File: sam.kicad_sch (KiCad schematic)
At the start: 46 parts, among them IC1 4164, IC15 MC6883, IC16 74LS244N, IC2 4164, IC3 4164, IC31 74LS02N, IC33 74LS138N, IC36 74LS132, IC37 GAL, IC4 4164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

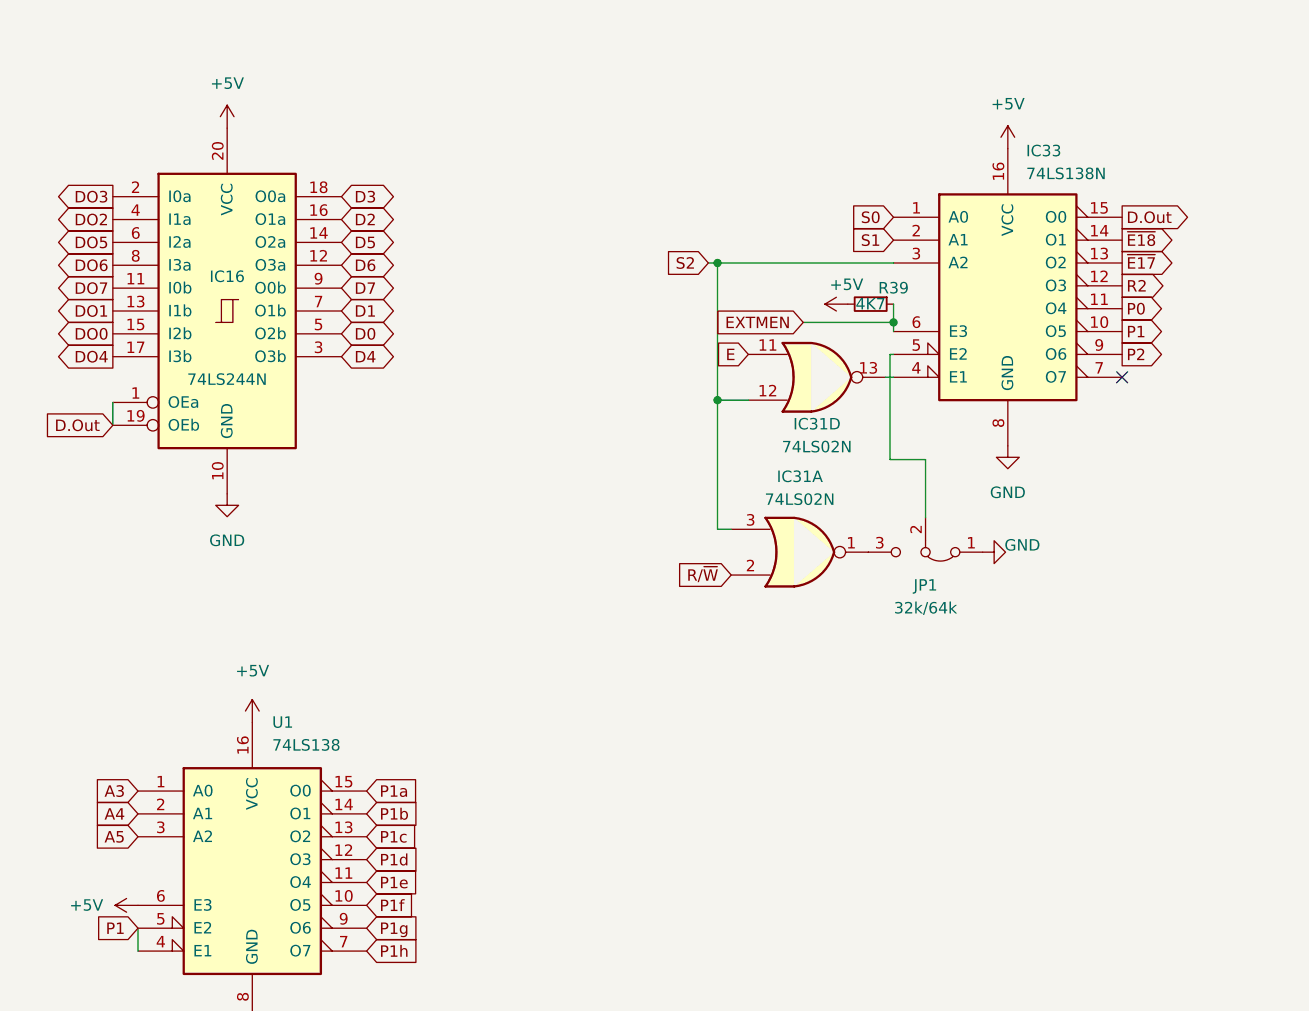
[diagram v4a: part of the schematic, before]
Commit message: fix rom and pia select traces
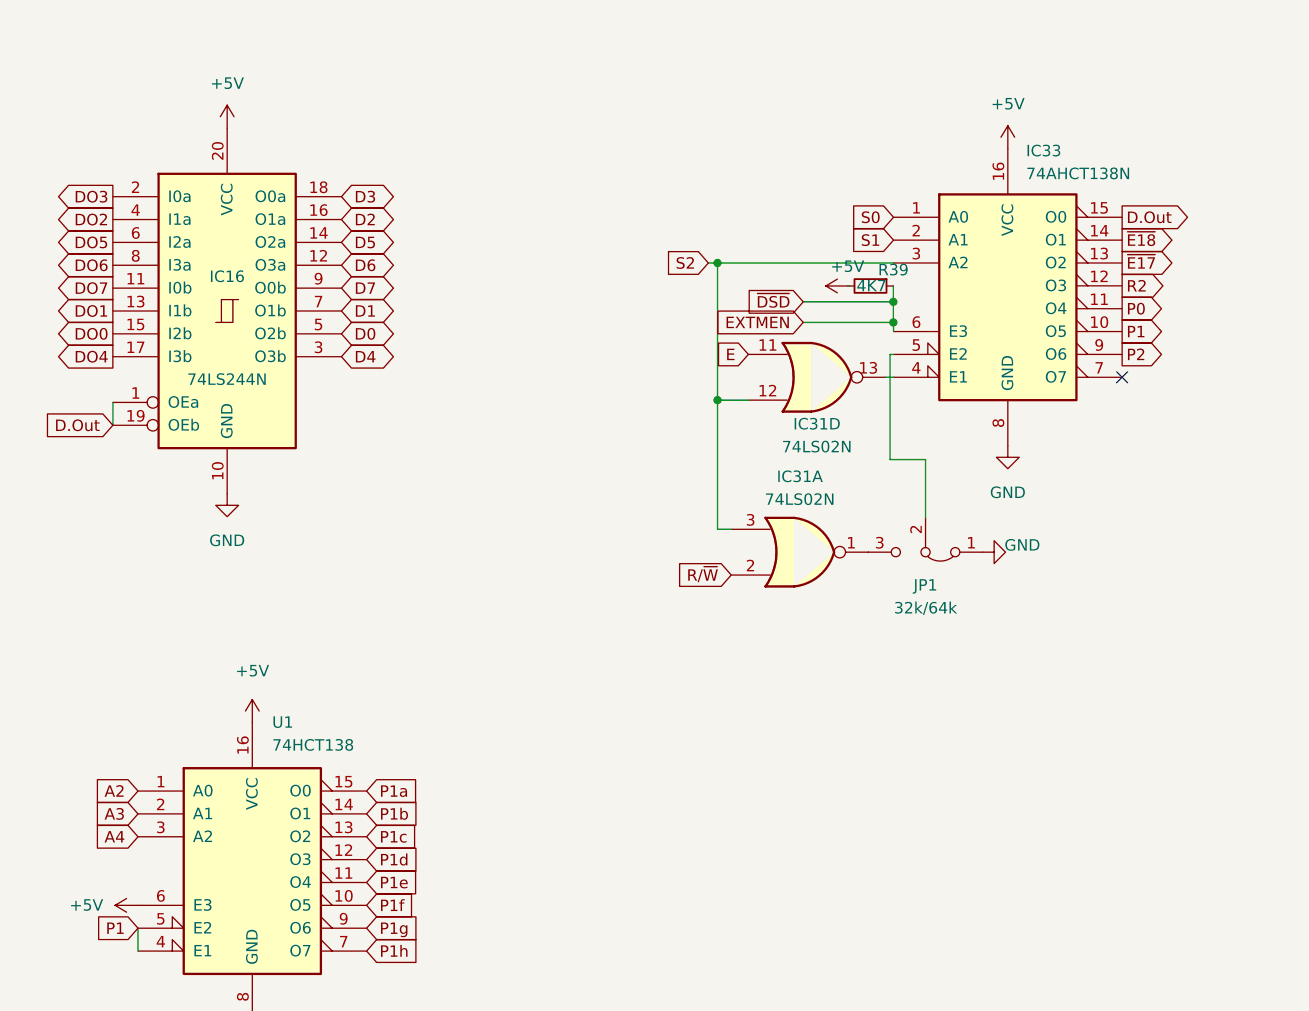
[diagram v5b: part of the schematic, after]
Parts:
- IC33: value 74LS138N -> 74AHCT138N
- JP5: footprint Jumper:SolderJumper-3_P1.3mm_Bridged12_Pad1.0x1.5mm -> Jumper:SolderJumper-3_P1.3mm_Open_Pad1.0x1.5mm
- U1: value 74LS138 -> 74HCT138
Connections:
- net ~{DSD} is gone; now on net EXTMEN: IC37.21 (IO2)
- net A2: now also U1.1 (A0)
- net A3: now also U1.2 (A1); no longer U1.1 (A0)
- net A4: now also U1.3 (A2); no longer U1.2 (A1)
- net A5: no longer U1.3 (A2)
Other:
- moved on the sheet: R39
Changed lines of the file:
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@@
     (comment 2 "Reposition dram and buffer")
   )
-  (junction (at 109.347 170.18) (diameter 0) (color 0 0 0 0)
+  (junction (at 109.3275 167.894) (diameter 0) (color 0 0 0 0)
   )
   (junction (at 66.929 24.638) (diameter 0) (color 0 0 0 0)
@@
   (junction (at 14.478 24.638) (diameter 0) (color 0 0 0 0)
   )
+  (junction (at 109.3275 170.18) (diameter 0) (color 0 0 0 0)
+  )
   (no_connect (at 134.747 176.276))
   (no_connect (at 259.842 177.292))
@@
     (stroke (width 0) (type default))
   )
+  (wire (pts (xy 99.314 167.894) (xy 109.3275 167.894))
+    (stroke (width 0) (type default))
+  )
   (wire (pts (xy 265.938 54.991) (xy 262.636 54.991))
     (stroke (width 0) (type default))
@@
     (stroke (width 0) (type default))
   )
+  (wire (pts (xy 109.3275 170.18) (xy 109.347 170.18))
+    (stroke (width 0) (type default))
+  )
   (wire (pts (xy 112.903 185.42) (xy 112.903 191.897))
     (stroke (width 0) (type default))
@@
     (stroke (width 0) (type default))
   )
+  (wire (pts (xy 104.3745 166.1319) (xy 104.2475 166.1319))
+    (stroke (width 0) (type default))
+  )
   (wire (pts (xy 93.218 178.816) (xy 89.789 178.816))
     (stroke (width 0) (type default))
@@
     (stroke (width 0) (type default))
   )
-  (wire (pts (xy 109.347 168.148) (xy 109.347 170.18))
+  (wire (pts (xy 109.3275 166.1319) (xy 109.3275 167.894))
     (stroke (width 0) (type default))
   )
@@
     (stroke (width 0) (type default))
   )
-  (wire (pts (xy 99.314 170.18) (xy 109.347 170.18))
+  (wire (pts (xy 109.3275 167.894) (xy 109.3275 170.18))
+    (stroke (width 0) (type default))
+  )
+  (wire (pts (xy 99.314 170.18) (xy 109.3275 170.18))
     (stroke (width 0) (type default))
   )
@@
     (stroke (width 0) (type default))
   )
-  (global_label "A5" (shape input) (at 25.4 227.33 180) (fields_autoplaced)
+  (global_label "A4" (shape input) (at 25.4 227.33 180) (fields_autoplaced)
     (effects (font (size 1.27 1.27)) (justify right))
     (property "Intersheetrefs" "${INTERSHEET_REFS}" (at 20.7709 227.33 0)
@@
     )
   )
+  (global_label "~{DSD}" (shape input) (at 99.314 167.894 180) (fields_autoplaced)
+    (effects (font (size 1.27 1.27)) (justify right))
+    (property "Intersheetrefs" "${INTERSHEET_REFS}" (at 93.2335 167.894 0)
+      (effects (font (size 1.27 1.27)) (justify right) hide)
+    )
+  )
   (global_label "RAM VCC" (shape passive) (at 168.148 146.431 0) (fields_autoplaced)
     (effects (font (size 1.27 1.27)) (justify left))
@@
     )
   )
-  (global_label "A3" (shape input) (at 25.4 222.25 180) (fields_autoplaced)
+  (global_label "A2" (shape input) (at 25.4 222.25 180) (fields_autoplaced)
     (effects (font (size 1.27 1.27)) (justify right))
     (property "Intersheetrefs" "${INTERSHEET_REFS}" (at 20.7709 222.25 0)
@@
     )
   )
-  (global_label "A4" (shape input) (at 25.4 224.79 180) (fields_autoplaced)
+  (global_label "A3" (shape input) (at 25.4 224.79 180) (fields_autoplaced)
     (effects (font (size 1.27 1.27)) (justify right))
     (property "Intersheetrefs" "${INTERSHEET_REFS}" (at 20.7709 224.79 0)
@@
       (effects (font (size 1.27 1.27)) (justify left))
     )
-    (property "Value" "74LS138" (at 40.2941 217.17 0)
+    (property "Value" "74HCT138" (at 40.2941 217.17 0)
       (effects (font (size 1.27 1.27)) (justify left))
     )
@@
       (effects (font (size 1.27 1.27)))
     )
-    (property "Footprint" "Jumper:SolderJumper-3_P1.3mm_Bridged12_Pad1.0x1.5mm" (at 207.518 39.116 0)
+    (property "Footprint" "Jumper:SolderJumper-3_P1.3mm_Open_Pad1.0x1.5mm" (at 207.518 39.116 0)
       (effects (font (size 1.27 1.27)) hide)
     )
@@
       (effects (font (size 1.27 1.27)) (justify left))
     )
-    (property "Value" "74LS138N" (at 124.0664 153.67 0)
+    (property "Value" "74AHCT138N" (at 124.0664 153.67 0)
       (effects (font (size 1.27 1.27)) (justify left))
     )
@@
     )
   )
-  (symbol (lib_id "Device:R_Small") (at 106.807 168.148 270) (unit 1)
+  (symbol (lib_id "Device:R_Small") (at 106.7875 166.1319 270) (unit 1)
     (in_bom yes) (on_board yes) (dnp no)
-    (property "Reference" "R39" (at 109.347 166.37 90)
+    (property "Reference" "R39" (at 109.3275 164.3539 90)
       (effects (font (size 1.27 1.27)))
     )
-    (property "Value" "4K7" (at 106.807 168.148 90)
+    (property "Value" "4K7" (at 106.9145 166.1319 90)
       (effects (font (size 1.27 1.27)))
     )
-    (property "Footprint" "Resistor_THT:R_Axial_DIN0207_L6.3mm_D2.5mm_P2.54mm_Vertical" (at 106.807 168.148 0)
+    (property "Footprint" "Resistor_THT:R_Axial_DIN0207_L6.3mm_D2.5mm_P2.54mm_Vertical" (at 106.7875 166.1319 0)
       (effects (font (size 1.27 1.27)) hide)
     )
-    (property "Datasheet" "~" (at 106.807 168.148 0)
+    (property "Datasheet" "~" (at 106.7875 166.1319 0)
       (effects (font (size 1.27 1.27)) hide)
     )
-    (property "DigiKey" "CF14JT4K70CT-ND" (at 106.807 168.148 0)
+    (property "DigiKey" "CF14JT4K70CT-ND" (at 106.7875 166.1319 0)
       (effects (font (size 1.27 1.27)) hide)
     )
@@
     )
   )
-  (symbol (lib_id "power:+5V") (at 104.267 168.148 90) (unit 1)
+  (symbol (lib_id "power:+5V") (at 104.3745 166.1319 90) (unit 1)
     (in_bom yes) (on_board yes) (dnp no)
-    (property "Reference" "#PWR0158" (at 108.077 168.148 0)
+    (property "Reference" "#PWR0158" (at 108.1845 166.1319 0)
       (effects (font (size 1.27 1.27)) hide)
     )
-    (property "Value" "+5V" (at 102.235 165.989 90)
+    (property "Value" "+5V" (at 102.3425 163.9729 90)
       (effects (font (size 1.27 1.27)) (justify right))
     )
-    (property "Footprint" "" (at 104.267 168.148 0)
+    (property "Footprint" "" (at 104.3745 166.1319 0)
       (effects (font (size 1.27 1.27)) hide)
     )
-    (property "Datasheet" "" (at 104.267 168.148 0)
+    (property "Datasheet" "" (at 104.3745 166.1319 0)
       (effects (font (size 1.27 1.27)) hide)
     )

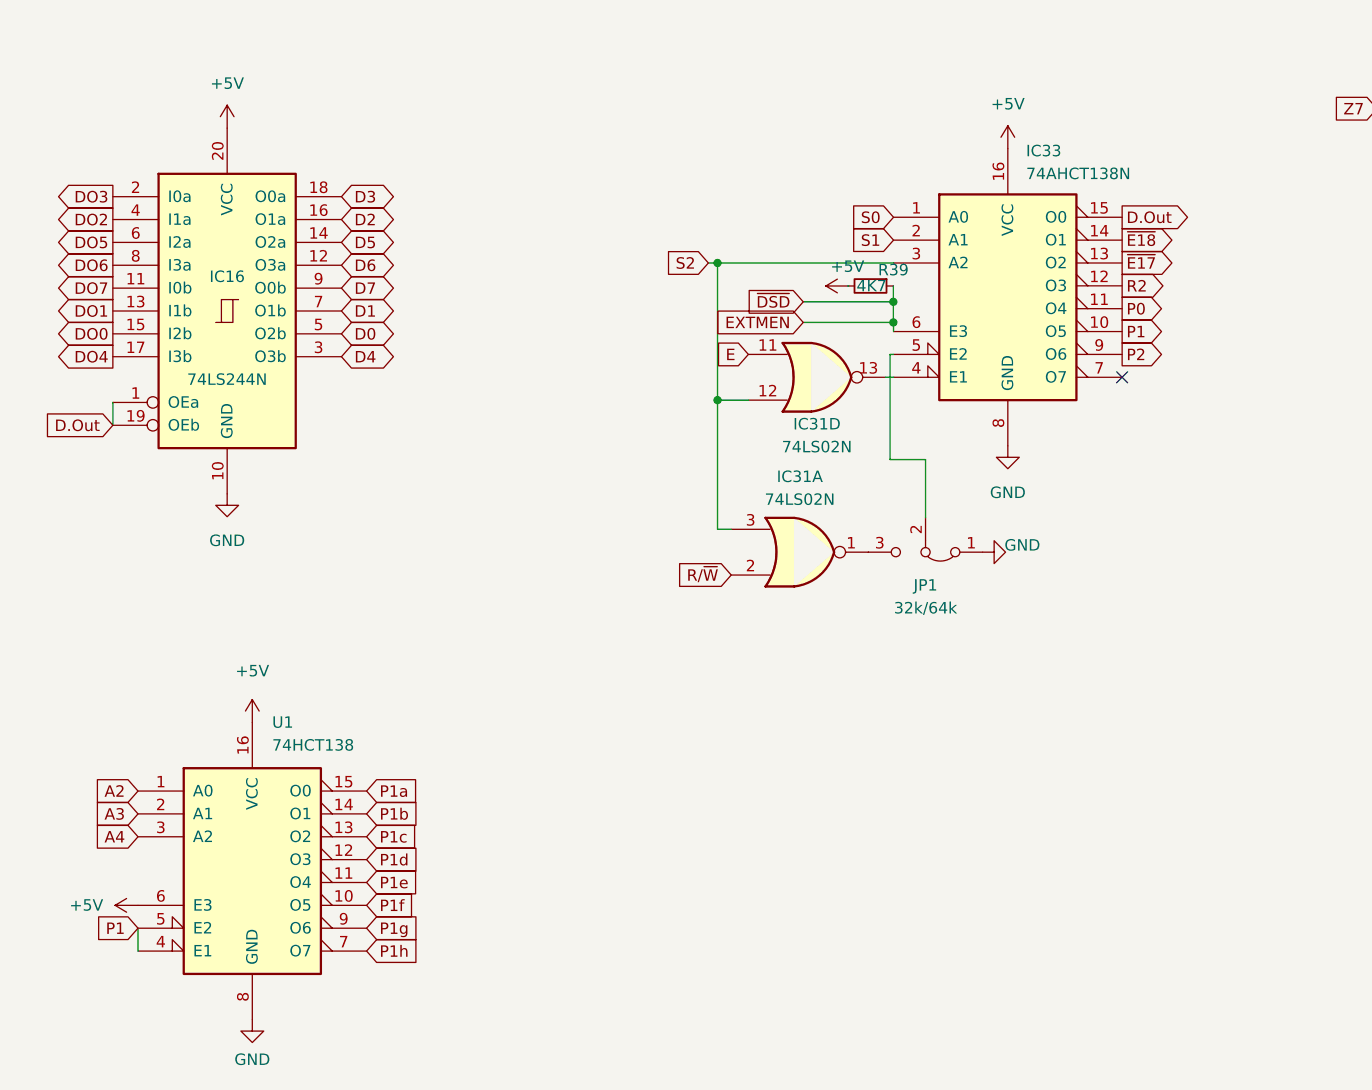
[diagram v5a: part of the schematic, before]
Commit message: reinforce audio traces
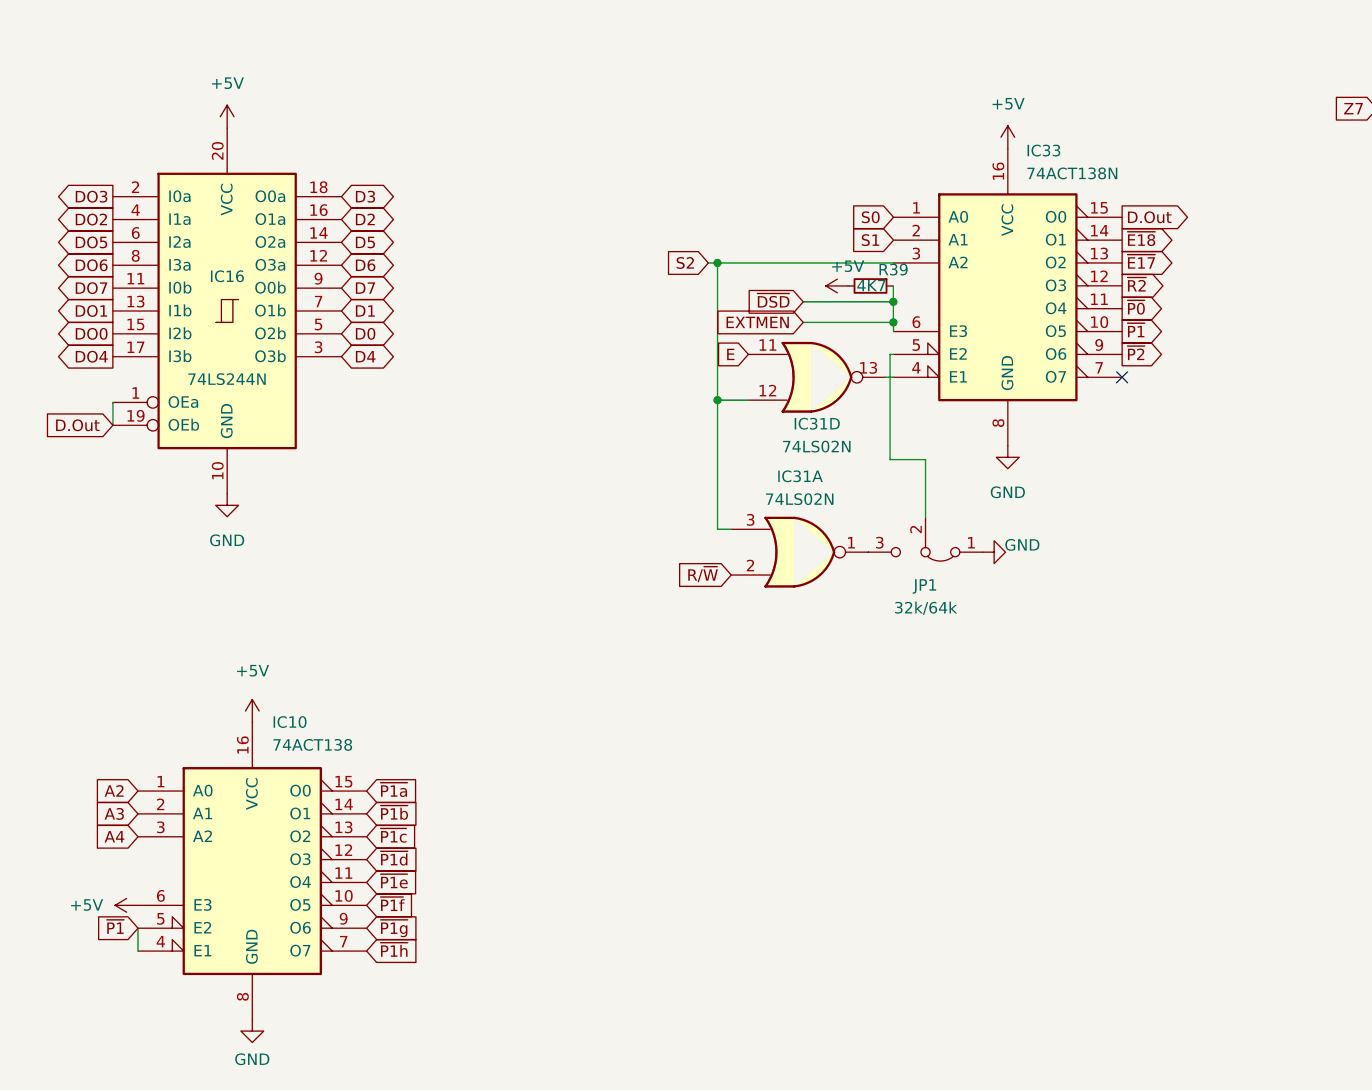
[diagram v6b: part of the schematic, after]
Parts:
- IC10: renamed from U1; value 74HCT138 -> 74ACT138
- IC33: value 74AHCT138N -> 74ACT138N
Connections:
- net P0 renamed ~{P0}
- net P1 renamed ~{P1}
- net P1a renamed ~{P1a}
- net P1b renamed ~{P1b}
- net P1c renamed ~{P1c}
- net P1d renamed ~{P1d}
- net P1e renamed ~{P1e}
- net P1f renamed ~{P1f}
- net P1g renamed ~{P1g}
- net P1h renamed ~{P1h}
- net P2 renamed ~{P2}
- net R2 renamed ~{R2}
